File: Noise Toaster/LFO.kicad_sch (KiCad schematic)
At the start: 16 parts, among them U2 LM324

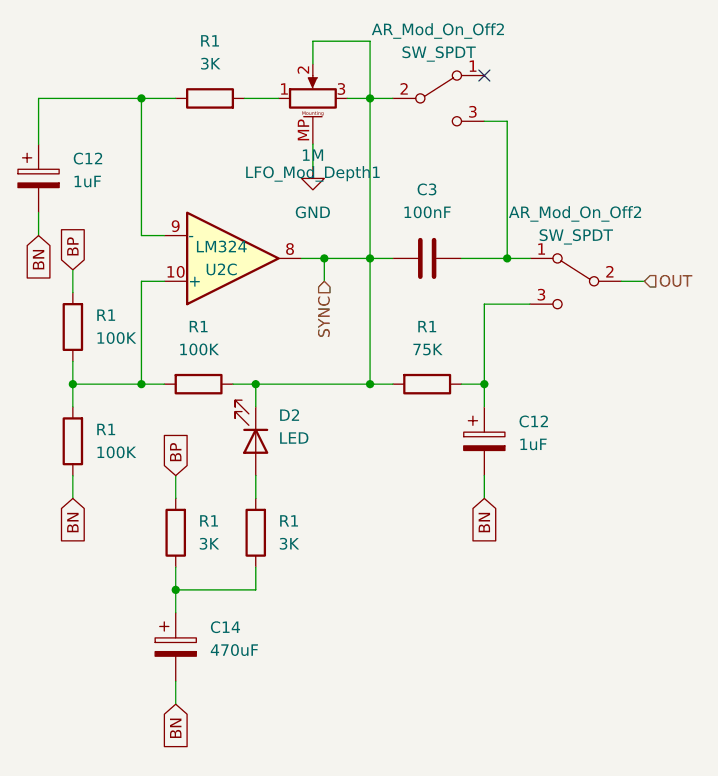
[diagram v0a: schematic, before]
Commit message: Noise Toaster - fixes after first board
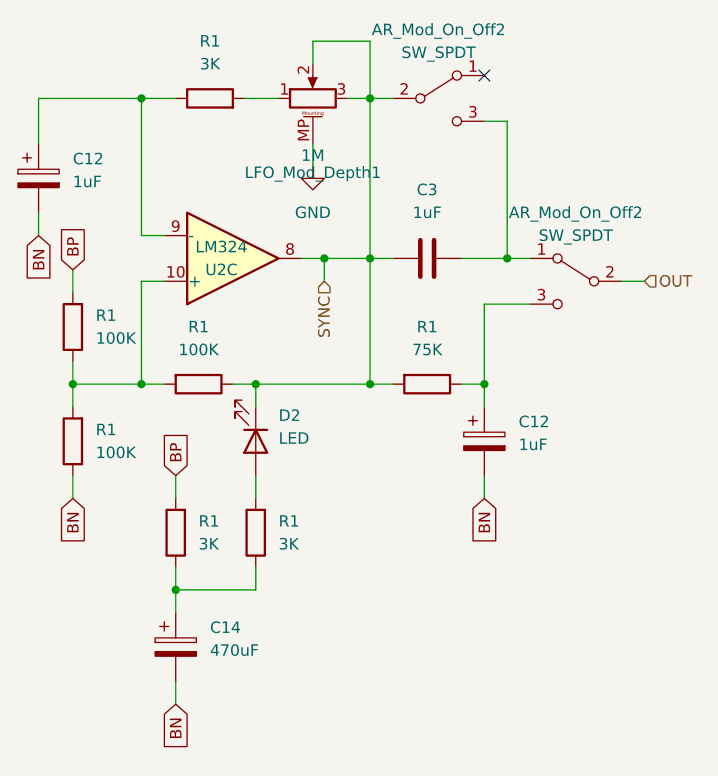
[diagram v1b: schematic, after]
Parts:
- C3: value 100nF -> 1uF; footprint Capacitor_THT:C_Disc_D3.0mm_W2.0mm_P2.50mm -> Capacitor_THT:C_Radial_D5.0mm_H7.0mm_P2.00mm
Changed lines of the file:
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@@
       (effects (font (size 1.27 1.27)))
     )
-    (property "Value" "100nF" (at 77.47 57.15 90)
+    (property "Value" "1uF" (at 77.47 57.15 90)
       (effects (font (size 1.27 1.27)))
     )
-    (property "Footprint" "Capacitor_THT:C_Disc_D3.0mm_W2.0mm_P2.50mm" (at 73.66 63.1952 0)
+    (property "Footprint" "Capacitor_THT:C_Radial_D5.0mm_H7.0mm_P2.00mm" (at 73.66 63.1952 0)
       (effects (font (size 1.27 1.27)) hide)
     )

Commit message: misc
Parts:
- renumbered C12 to C17, C14 to C18, C3 to C19, C12 to C20, LFO_Mod_Depth1 to LFO_RATE1, AR_Mod_On_Off2 to LFO_SHAPE1, AR_Mod_On_Off2 to LFO_SHAPE2, R1 to R42, R1 to R43, R1 to R44, R1 to R45, R1 to R46, R1 to R47, R1 to R48
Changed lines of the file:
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@@
   (symbol (lib_id "Device:C_Polarized") (at 49.53 105.41 0) (unit 1)
     (in_bom yes) (on_board yes) (dnp no) (fields_autoplaced)
-    (property "Reference" "C14" (at 53.34 103.251 0)
+    (property "Reference" "C18" (at 53.34 103.251 0)
       (effects (font (size 1.27 1.27)) (justify left))
     )
@@
     (instances
       (project "Noise Toaster"
-        (path "/c06bdaff-9d92-4322-9a29-784b2d9ec2c6/46712425-f81c-4e59-b8d1-7e996aa9ca64"
-          (reference "C14") (unit 1)
-        )
         (path "/c06bdaff-9d92-4322-9a29-784b2d9ec2c6/74bc29e1-6bfb-4a22-9659-b607bacf38d2"
           (reference "C18") (unit 1)
@@
   (symbol (lib_id "Device:R") (at 58.42 92.71 180) (unit 1)
     (in_bom yes) (on_board yes) (dnp no) (fields_autoplaced)
-    (property "Reference" "R1" (at 60.96 91.44 0)
+    (property "Reference" "R47" (at 60.96 91.44 0)
       (effects (font (size 1.27 1.27)) (justify right))
     )
@@
     (instances
       (project "Noise Toaster"
-        (path "/c06bdaff-9d92-4322-9a29-784b2d9ec2c6/3f36173e-f191-4036-853e-444de7299fbe"
-          (reference "R1") (unit 1)
-        )
         (path "/c06bdaff-9d92-4322-9a29-784b2d9ec2c6/74bc29e1-6bfb-4a22-9659-b607bacf38d2"
           (reference "R47") (unit 1)
@@
   (symbol (lib_id "Device:C") (at 77.47 62.23 270) (unit 1)
     (in_bom yes) (on_board yes) (dnp no) (fields_autoplaced)
-    (property "Reference" "C3" (at 77.47 54.61 90)
+    (property "Reference" "C19" (at 77.47 54.61 90)
       (effects (font (size 1.27 1.27)))
     )
@@
     (instances
       (project "Noise Toaster"
-        (path "/c06bdaff-9d92-4322-9a29-784b2d9ec2c6/3f36173e-f191-4036-853e-444de7299fbe"
-          (reference "C3") (unit 1)
-        )
         (path "/c06bdaff-9d92-4322-9a29-784b2d9ec2c6/74bc29e1-6bfb-4a22-9659-b607bacf38d2"
           (reference "C19") (unit 1)
@@
   (symbol (lib_id "Device:R") (at 52.07 76.2 270) (unit 1)
     (in_bom yes) (on_board yes) (dnp no) (fields_autoplaced)
-    (property "Reference" "R1" (at 52.07 69.85 90)
+    (property "Reference" "R45" (at 52.07 69.85 90)
       (effects (font (size 1.27 1.27)))
     )
@@
     (instances
       (project "Noise Toaster"
-        (path "/c06bdaff-9d92-4322-9a29-784b2d9ec2c6/3f36173e-f191-4036-853e-444de7299fbe"
-          (reference "R1") (unit 1)
-        )
         (path "/c06bdaff-9d92-4322-9a29-784b2d9ec2c6/74bc29e1-6bfb-4a22-9659-b607bacf38d2"
           (reference "R45") (unit 1)
@@
   (symbol (lib_id "Device:R") (at 38.1 69.85 180) (unit 1)
     (in_bom yes) (on_board yes) (dnp no) (fields_autoplaced)
-    (property "Reference" "R1" (at 40.64 68.58 0)
+    (property "Reference" "R42" (at 40.64 68.58 0)
       (effects (font (size 1.27 1.27)) (justify right))
     )
@@
     (instances
       (project "Noise Toaster"
-        (path "/c06bdaff-9d92-4322-9a29-784b2d9ec2c6/3f36173e-f191-4036-853e-444de7299fbe"
-          (reference "R1") (unit 1)
-        )
         (path "/c06bdaff-9d92-4322-9a29-784b2d9ec2c6/74bc29e1-6bfb-4a22-9659-b607bacf38d2"
           (reference "R42") (unit 1)
@@
   (symbol (lib_id "Device:R") (at 53.34 44.45 90) (unit 1)
     (in_bom yes) (on_board yes) (dnp no) (fields_autoplaced)
-    (property "Reference" "R1" (at 53.34 38.1 90)
+    (property "Reference" "R46" (at 53.34 38.1 90)
       (effects (font (size 1.27 1.27)))
     )
@@
     (instances
       (project "Noise Toaster"
-        (path "/c06bdaff-9d92-4322-9a29-784b2d9ec2c6/3f36173e-f191-4036-853e-444de7299fbe"
-          (reference "R1") (unit 1)
-        )
         (path "/c06bdaff-9d92-4322-9a29-784b2d9ec2c6/74bc29e1-6bfb-4a22-9659-b607bacf38d2"
           (reference "R46") (unit 1)
@@
     (instances
       (project "Noise Toaster"
-        (path "/c06bdaff-9d92-4322-9a29-784b2d9ec2c6/3f36173e-f191-4036-853e-444de7299fbe"
+        (path "/c06bdaff-9d92-4322-9a29-784b2d9ec2c6/74bc29e1-6bfb-4a22-9659-b607bacf38d2"
           (reference "U2") (unit 3)
         )
-        (path "/c06bdaff-9d92-4322-9a29-784b2d9ec2c6/46712425-f81c-4e59-b8d1-7e996aa9ca64"
-          (reference "U2") (unit 3)
-        )
-        (path "/c06bdaff-9d92-4322-9a29-784b2d9ec2c6/74bc29e1-6bfb-4a22-9659-b607bacf38d2"
-          (reference "U2") (unit 3)
-        )
       )
     )
@@
   (symbol (lib_id "Device:R") (at 49.53 92.71 180) (unit 1)
     (in_bom yes) (on_board yes) (dnp no) (fields_autoplaced)
-    (property "Reference" "R1" (at 52.07 91.44 0)
+    (property "Reference" "R44" (at 52.07 91.44 0)
       (effects (font (size 1.27 1.27)) (justify right))
     )
@@
     (instances
       (project "Noise Toaster"
-        (path "/c06bdaff-9d92-4322-9a29-784b2d9ec2c6/3f36173e-f191-4036-853e-444de7299fbe"
-          (reference "R1") (unit 1)
-        )
         (path "/c06bdaff-9d92-4322-9a29-784b2d9ec2c6/74bc29e1-6bfb-4a22-9659-b607bacf38d2"
           (reference "R44") (unit 1)
@@
   (symbol (lib_id "Device:C_Polarized") (at 34.29 53.34 0) (unit 1)
     (in_bom yes) (on_board yes) (dnp no) (fields_autoplaced)
-    (property "Reference" "C12" (at 38.1 51.181 0)
+    (property "Reference" "C17" (at 38.1 51.181 0)
       (effects (font (size 1.27 1.27)) (justify left))
     )
@@
     (instances
       (project "Noise Toaster"
-        (path "/c06bdaff-9d92-4322-9a29-784b2d9ec2c6/46712425-f81c-4e59-b8d1-7e996aa9ca64"
-          (reference "C12") (unit 1)
-        )
         (path "/c06bdaff-9d92-4322-9a29-784b2d9ec2c6/74bc29e1-6bfb-4a22-9659-b607bacf38d2"
           (reference "C17") (unit 1)
@@
   (symbol (lib_id "Device:R") (at 77.47 76.2 270) (unit 1)
     (in_bom yes) (on_board yes) (dnp no) (fields_autoplaced)
-    (property "Reference" "R1" (at 77.47 69.85 90)
+    (property "Reference" "R48" (at 77.47 69.85 90)
       (effects (font (size 1.27 1.27)))
     )
@@
     (instances
       (project "Noise Toaster"
-        (path "/c06bdaff-9d92-4322-9a29-784b2d9ec2c6/3f36173e-f191-4036-853e-444de7299fbe"
-          (reference "R1") (unit 1)
-        )
         (path "/c06bdaff-9d92-4322-9a29-784b2d9ec2c6/74bc29e1-6bfb-4a22-9659-b607bacf38d2"
           (reference "R48") (unit 1)
@@
   (symbol (lib_id "power:GND") (at 64.77 52.07 0) (unit 1)
     (in_bom yes) (on_board yes) (dnp no) (fields_autoplaced)
-    (property "Reference" "#PWR04" (at 64.77 58.42 0)
+    (property "Reference" "#PWR014" (at 64.77 58.42 0)
       (effects (font (size 1.27 1.27)) hide)
     )
@@
     (instances
       (project "Noise Toaster"
-        (path "/c06bdaff-9d92-4322-9a29-784b2d9ec2c6/3f36173e-f191-4036-853e-444de7299fbe"
-          (reference "#PWR04") (unit 1)
-        )
         (path "/c06bdaff-9d92-4322-9a29-784b2d9ec2c6/74bc29e1-6bfb-4a22-9659-b607bacf38d2"
           (reference "#PWR014") (unit 1)
@@
   (symbol (lib_id "Device:R") (at 38.1 82.55 180) (unit 1)
     (in_bom yes) (on_board yes) (dnp no) (fields_autoplaced)
-    (property "Reference" "R1" (at 40.64 81.28 0)
+    (property "Reference" "R43" (at 40.64 81.28 0)
       (effects (font (size 1.27 1.27)) (justify right))
     )
@@
     (instances
       (project "Noise Toaster"
-        (path "/c06bdaff-9d92-4322-9a29-784b2d9ec2c6/3f36173e-f191-4036-853e-444de7299fbe"
-          (reference "R1") (unit 1)
-        )
         (path "/c06bdaff-9d92-4322-9a29-784b2d9ec2c6/74bc29e1-6bfb-4a22-9659-b607bacf38d2"
           (reference "R43") (unit 1)
@@
   (symbol (lib_id "Device:C_Polarized") (at 83.82 82.55 0) (unit 1)
     (in_bom yes) (on_board yes) (dnp no) (fields_autoplaced)
-    (property "Reference" "C12" (at 87.63 80.391 0)
+    (property "Reference" "C20" (at 87.63 80.391 0)
       (effects (font (size 1.27 1.27)) (justify left))
     )
@@
     (instances
       (project "Noise Toaster"
-        (path "/c06bdaff-9d92-4322-9a29-784b2d9ec2c6/46712425-f81c-4e59-b8d1-7e996aa9ca64"
-          (reference "C12") (unit 1)
-        )
         (path "/c06bdaff-9d92-4322-9a29-784b2d9ec2c6/74bc29e1-6bfb-4a22-9659-b607bacf38d2"
           (reference "C20") (unit 1)
@@
   (symbol (lib_id "Switch:SW_SPDT") (at 78.74 44.45 0) (unit 1)
     (in_bom yes) (on_board yes) (dnp no)
-    (property "Reference" "AR_Mod_On_Off2" (at 78.74 36.83 0)
+    (property "Reference" "LFO_SHAPE1" (at 78.74 36.83 0)
       (effects (font (size 1.27 1.27)))
     )
@@
     (instances
       (project "Noise Toaster"
-        (path "/c06bdaff-9d92-4322-9a29-784b2d9ec2c6/3f36173e-f191-4036-853e-444de7299fbe"
-          (reference "AR_Mod_On_Off2") (unit 1)
-        )
         (path "/c06bdaff-9d92-4322-9a29-784b2d9ec2c6/74bc29e1-6bfb-4a22-9659-b607bacf38d2"
           (reference "LFO_SHAPE1") (unit 1)
@@
   (symbol (lib_id "Device:R_Potentiometer_MountingPin") (at 64.77 44.45 90) (unit 1)
     (in_bom yes) (on_board yes) (dnp no)
-    (property "Reference" "LFO_Mod_Depth1" (at 64.77 52.705 90)
+    (property "Reference" "LFO_RATE1" (at 64.77 52.705 90)
       (effects (font (size 1.27 1.27)))
     )
@@
     (instances
       (project "Noise Toaster"
-        (path "/c06bdaff-9d92-4322-9a29-784b2d9ec2c6/3f36173e-f191-4036-853e-444de7299fbe"
-          (reference "LFO_Mod_Depth1") (unit 1)
-        )
         (path "/c06bdaff-9d92-4322-9a29-784b2d9ec2c6/74bc29e1-6bfb-4a22-9659-b607bacf38d2"
           (reference "LFO_RATE1") (unit 1)
@@
   (symbol (lib_id "Switch:SW_SPDT") (at 93.98 64.77 0) (mirror y) (unit 1)
     (in_bom yes) (on_board yes) (dnp no)
-    (property "Reference" "AR_Mod_On_Off2" (at 93.98 57.15 0)
+    (property "Reference" "LFO_SHAPE2" (at 93.98 57.15 0)
       (effects (font (size 1.27 1.27)))
     )
@@
     (instances
       (project "Noise Toaster"
-        (path "/c06bdaff-9d92-4322-9a29-784b2d9ec2c6/3f36173e-f191-4036-853e-444de7299fbe"
-          (reference "AR_Mod_On_Off2") (unit 1)
-        )
         (path "/c06bdaff-9d92-4322-9a29-784b2d9ec2c6/74bc29e1-6bfb-4a22-9659-b607bacf38d2"
           (reference "LFO_SHAPE2") (unit 1)
